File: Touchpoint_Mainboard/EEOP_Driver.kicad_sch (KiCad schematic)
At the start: 3 parts, among them J4 Conn_01x32, J5 Conn_01x32, U9 HV507PG-G

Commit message: Finished assigning most footprints
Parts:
- J4, J5: footprint (none) -> Touchpoint:HRS_FH34SRJ-32S-0.5SH_50_
- U9: footprint PQFP80_20X14MC_MCH -> Touchpoint:PQFP80_20X14MC_MCH
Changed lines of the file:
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@@
 			)
 		)
-		(property "Footprint" ""
+		(property "Footprint" "Touchpoint:HRS_FH34SRJ-32S-0.5SH_50_"
 			(at 116.84 57.15 0)
 			(effects
@@
 			)
 		)
-		(property "Footprint" ""
+		(property "Footprint" "Touchpoint:HRS_FH34SRJ-32S-0.5SH_50_"
 			(at 149.86 55.88 0)
 			(effects
@@
 			)
 		)
-		(property "Footprint" "PQFP80_20X14MC_MCH"
+		(property "Footprint" "Touchpoint:PQFP80_20X14MC_MCH"
 			(at 26.67 24.13 0)
 			(effects

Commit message: Finished assigning footprints and 3d models for both boards
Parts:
- U9: footprint Touchpoint:PQFP80_20X14MC_MCH -> Package_QFP:PQFP-80_14x20mm_P0.8mm
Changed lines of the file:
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@@
 			)
 		)
-		(property "Footprint" "Touchpoint:PQFP80_20X14MC_MCH"
+		(property "Footprint" "Package_QFP:PQFP-80_14x20mm_P0.8mm"
 			(at 26.67 24.13 0)
 			(effects

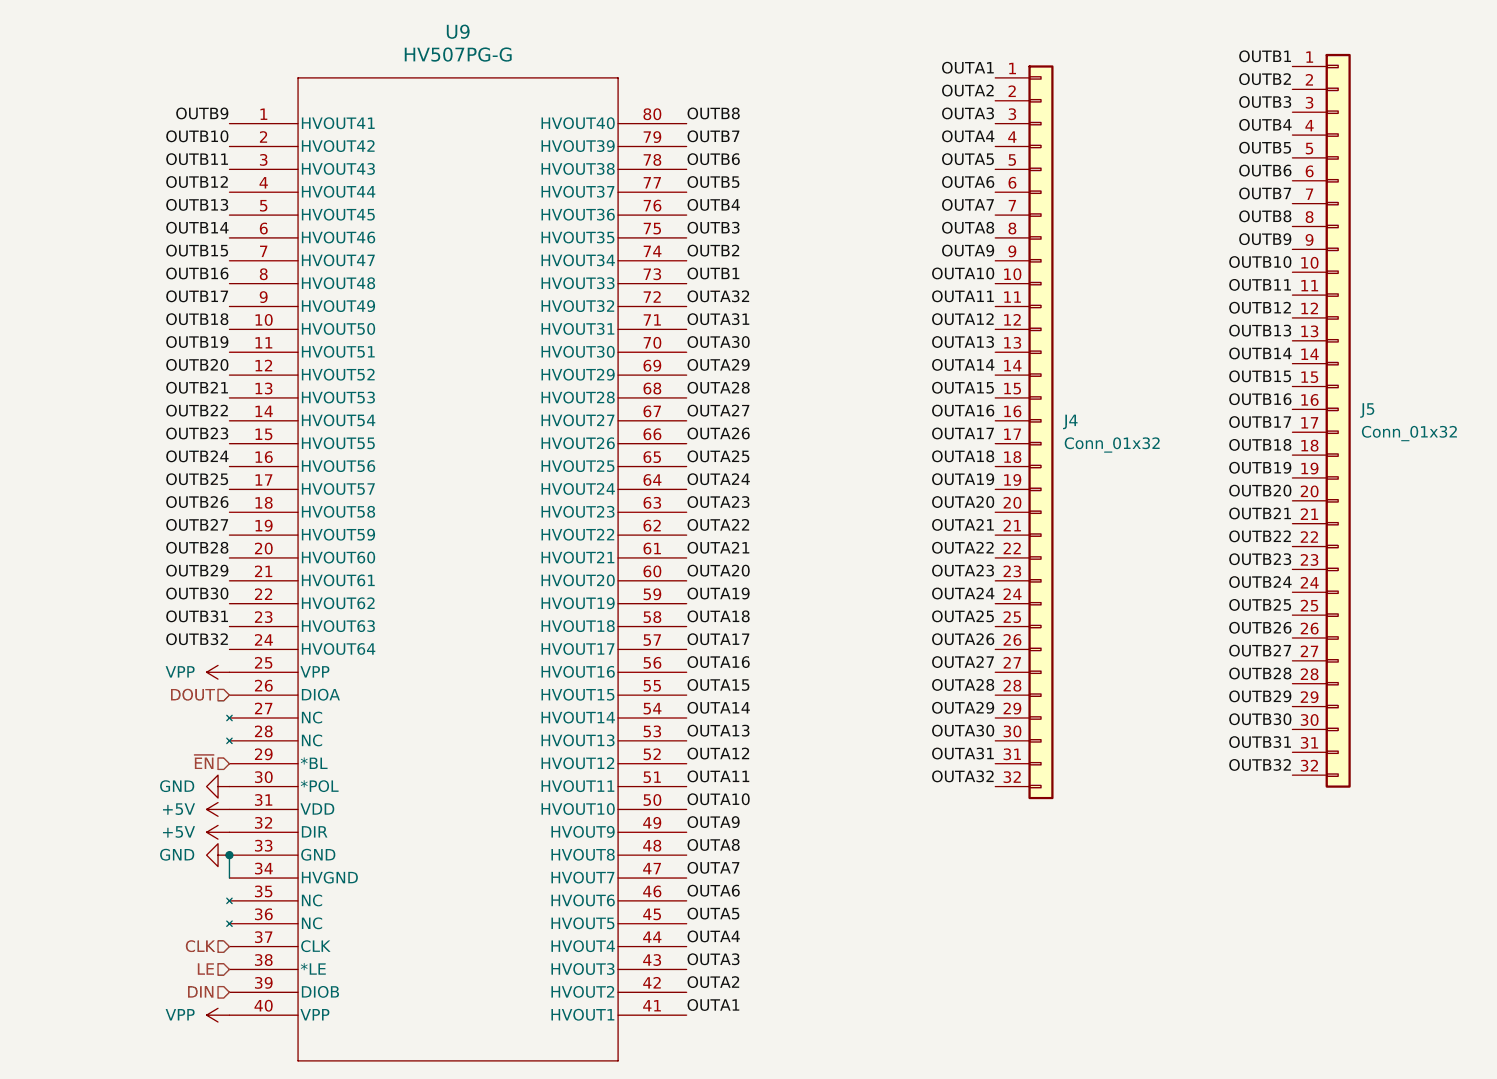
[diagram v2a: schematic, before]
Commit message: Added 3.3V to interface
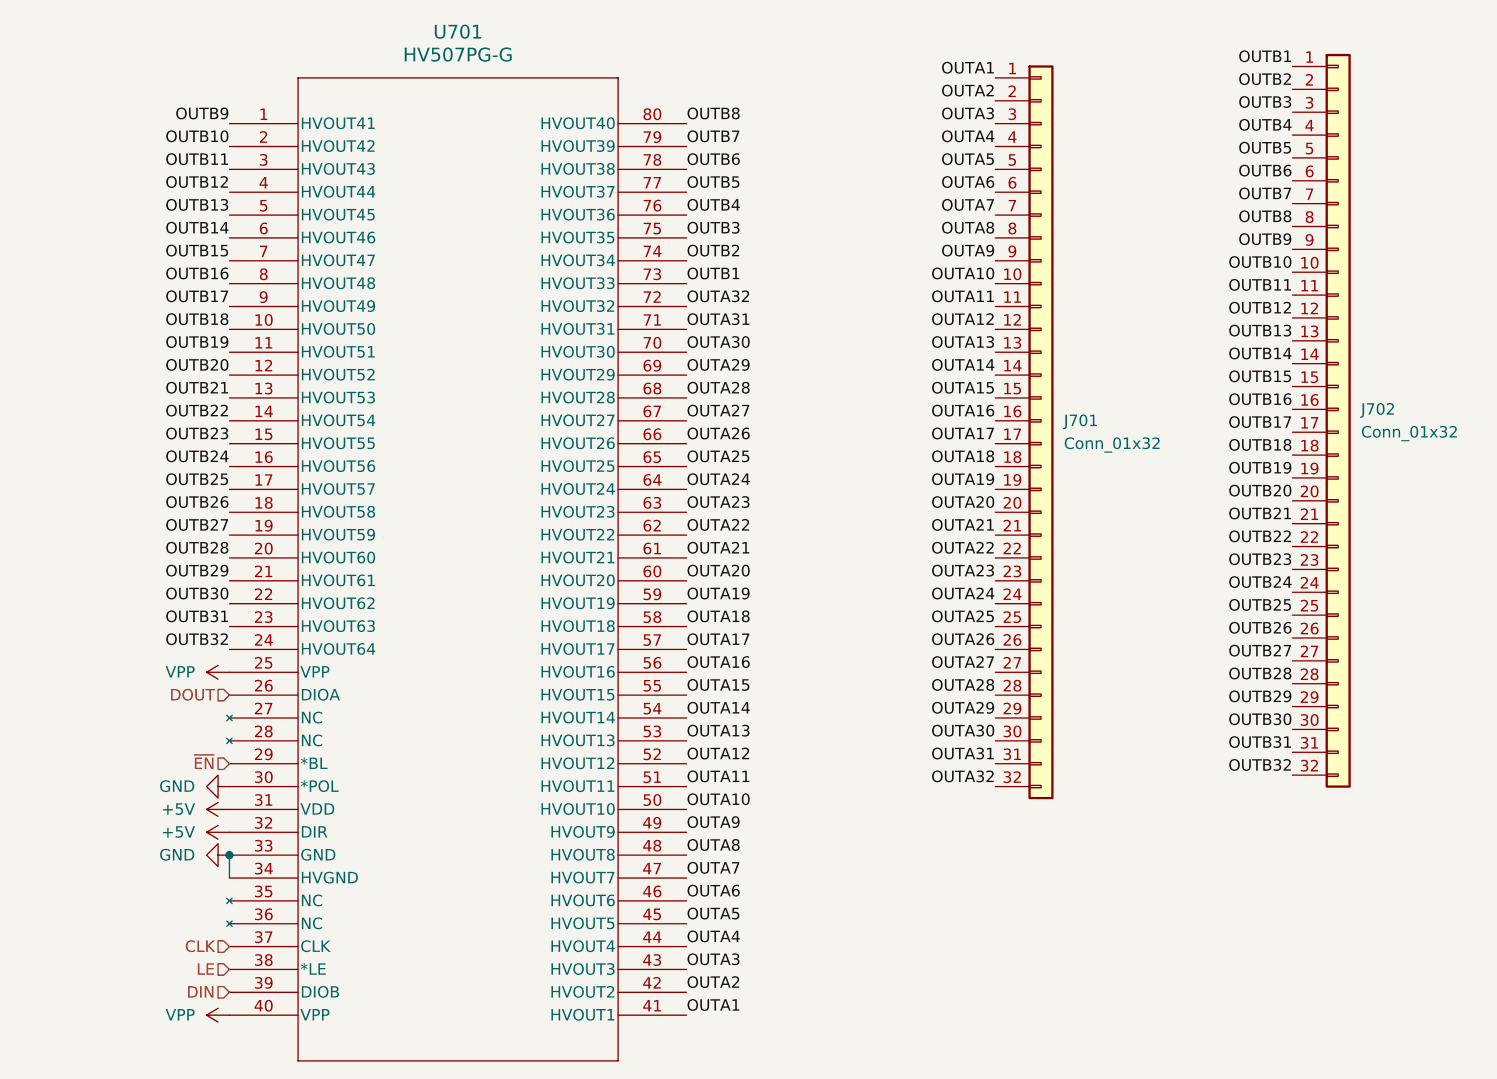
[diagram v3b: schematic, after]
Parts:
- renumbered J4 to J701, J5 to J702, U9 to U701
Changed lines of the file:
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@@
 		(dnp no)
 		(fields_autoplaced yes)
-		(property "Reference" "#PWR066"
+		(property "Reference" "#PWR0705"
 			(at 20.32 105.41 0)
 			(effects
@@
 			(project ""
 				(path "/f37b5f88-420a-4646-85df-8f9851d23e3c/d77d4631-394e-42d9-bdcc-1bd3eb66f861"
-					(reference "#PWR066")
+					(reference "#PWR0705")
 					(unit 1)
 				)
@@
 		(dnp no)
 		(fields_autoplaced yes)
-		(property "Reference" "#PWR078"
+		(property "Reference" "#PWR0702"
 			(at 20.32 97.79 0)
 			(effects
@@
 			(project "Touchpoint_Mainboard"
 				(path "/f37b5f88-420a-4646-85df-8f9851d23e3c/d77d4631-394e-42d9-bdcc-1bd3eb66f861"
-					(reference "#PWR078")
+					(reference "#PWR0702")
 					(unit 1)
 				)
@@
 		(dnp no)
 		(fields_autoplaced yes)
-		(property "Reference" "#PWR077"
+		(property "Reference" "#PWR0704"
 			(at 30.48 102.87 0)
 			(effects
@@
 			(project "Touchpoint_Mainboard"
 				(path "/f37b5f88-420a-4646-85df-8f9851d23e3c/d77d4631-394e-42d9-bdcc-1bd3eb66f861"
-					(reference "#PWR077")
+					(reference "#PWR0704")
 					(unit 1)
 				)
@@
 		(dnp no)
 		(fields_autoplaced yes)
-		(property "Reference" "J4"
+		(property "Reference" "J701"
 			(at 119.38 57.1499 0)
 			(effects
@@
 			(project ""
 				(path "/f37b5f88-420a-4646-85df-8f9851d23e3c/d77d4631-394e-42d9-bdcc-1bd3eb66f861"
-					(reference "J4")
+					(reference "J701")
 					(unit 1)
 				)
@@
 		(dnp no)
 		(fields_autoplaced yes)
-		(property "Reference" "J5"
+		(property "Reference" "J702"
 			(at 152.4 55.8799 0)
 			(effects
@@
 			(project "Touchpoint_Mainboard"
 				(path "/f37b5f88-420a-4646-85df-8f9851d23e3c/d77d4631-394e-42d9-bdcc-1bd3eb66f861"
-					(reference "J5")
+					(reference "J702")
 					(unit 1)
 				)
@@
 		(dnp no)
 		(fields_autoplaced yes)
-		(property "Reference" "#PWR079"
+		(property "Reference" "#PWR0706"
 			(at 30.48 123.19 0)
 			(effects
@@
 			(project ""
 				(path "/f37b5f88-420a-4646-85df-8f9851d23e3c/d77d4631-394e-42d9-bdcc-1bd3eb66f861"
-					(reference "#PWR079")
+					(reference "#PWR0706")
 					(unit 1)
 				)
@@
 		(dnp no)
 		(fields_autoplaced yes)
-		(property "Reference" "#PWR076"
+		(property "Reference" "#PWR0703"
 			(at 30.48 100.33 0)
 			(effects
@@
 			(project ""
 				(path "/f37b5f88-420a-4646-85df-8f9851d23e3c/d77d4631-394e-42d9-bdcc-1bd3eb66f861"
-					(reference "#PWR076")
+					(reference "#PWR0703")
 					(unit 1)
 				)
@@
 		(dnp no)
 		(fields_autoplaced yes)
-		(property "Reference" "U9"
+		(property "Reference" "U701"
 			(at 52.07 13.97 0)
 			(effects
@@
 			(project ""
 				(path "/f37b5f88-420a-4646-85df-8f9851d23e3c/d77d4631-394e-42d9-bdcc-1bd3eb66f861"
-					(reference "U9")
+					(reference "U701")
 					(unit 1)
 				)
@@
 		(dnp no)
 		(fields_autoplaced yes)
-		(property "Reference" "#PWR080"
+		(property "Reference" "#PWR0701"
 			(at 30.48 85.09 0)
 			(effects
@@
 			(project "Touchpoint_Mainboard"
 				(path "/f37b5f88-420a-4646-85df-8f9851d23e3c/d77d4631-394e-42d9-bdcc-1bd3eb66f861"
-					(reference "#PWR080")
+					(reference "#PWR0701")
 					(unit 1)
 				)

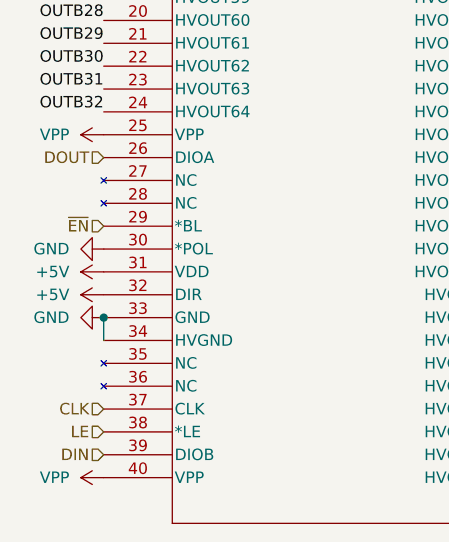
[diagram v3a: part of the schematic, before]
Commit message: Working through mainboard routing
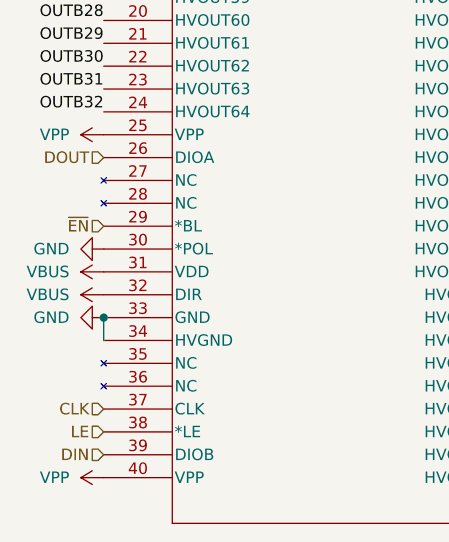
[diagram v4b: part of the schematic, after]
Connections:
- net +5V renamed VBUS
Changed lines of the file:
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@@
 			)
 		)
-		(property "Value" "+5V"
+		(property "Value" "VBUS"
 			(at 22.86 102.8699 90)
 			(effects
@@
 			)
 		)
-		(property "Value" "+5V"
+		(property "Value" "VBUS"
 			(at 22.86 100.3299 90)
 			(effects
